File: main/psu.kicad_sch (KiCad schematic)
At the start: 33 parts, among them U401 TSV911xxLx, U402 LMR51430, U403 LDK130M33R, U404 LM317_SOT-223

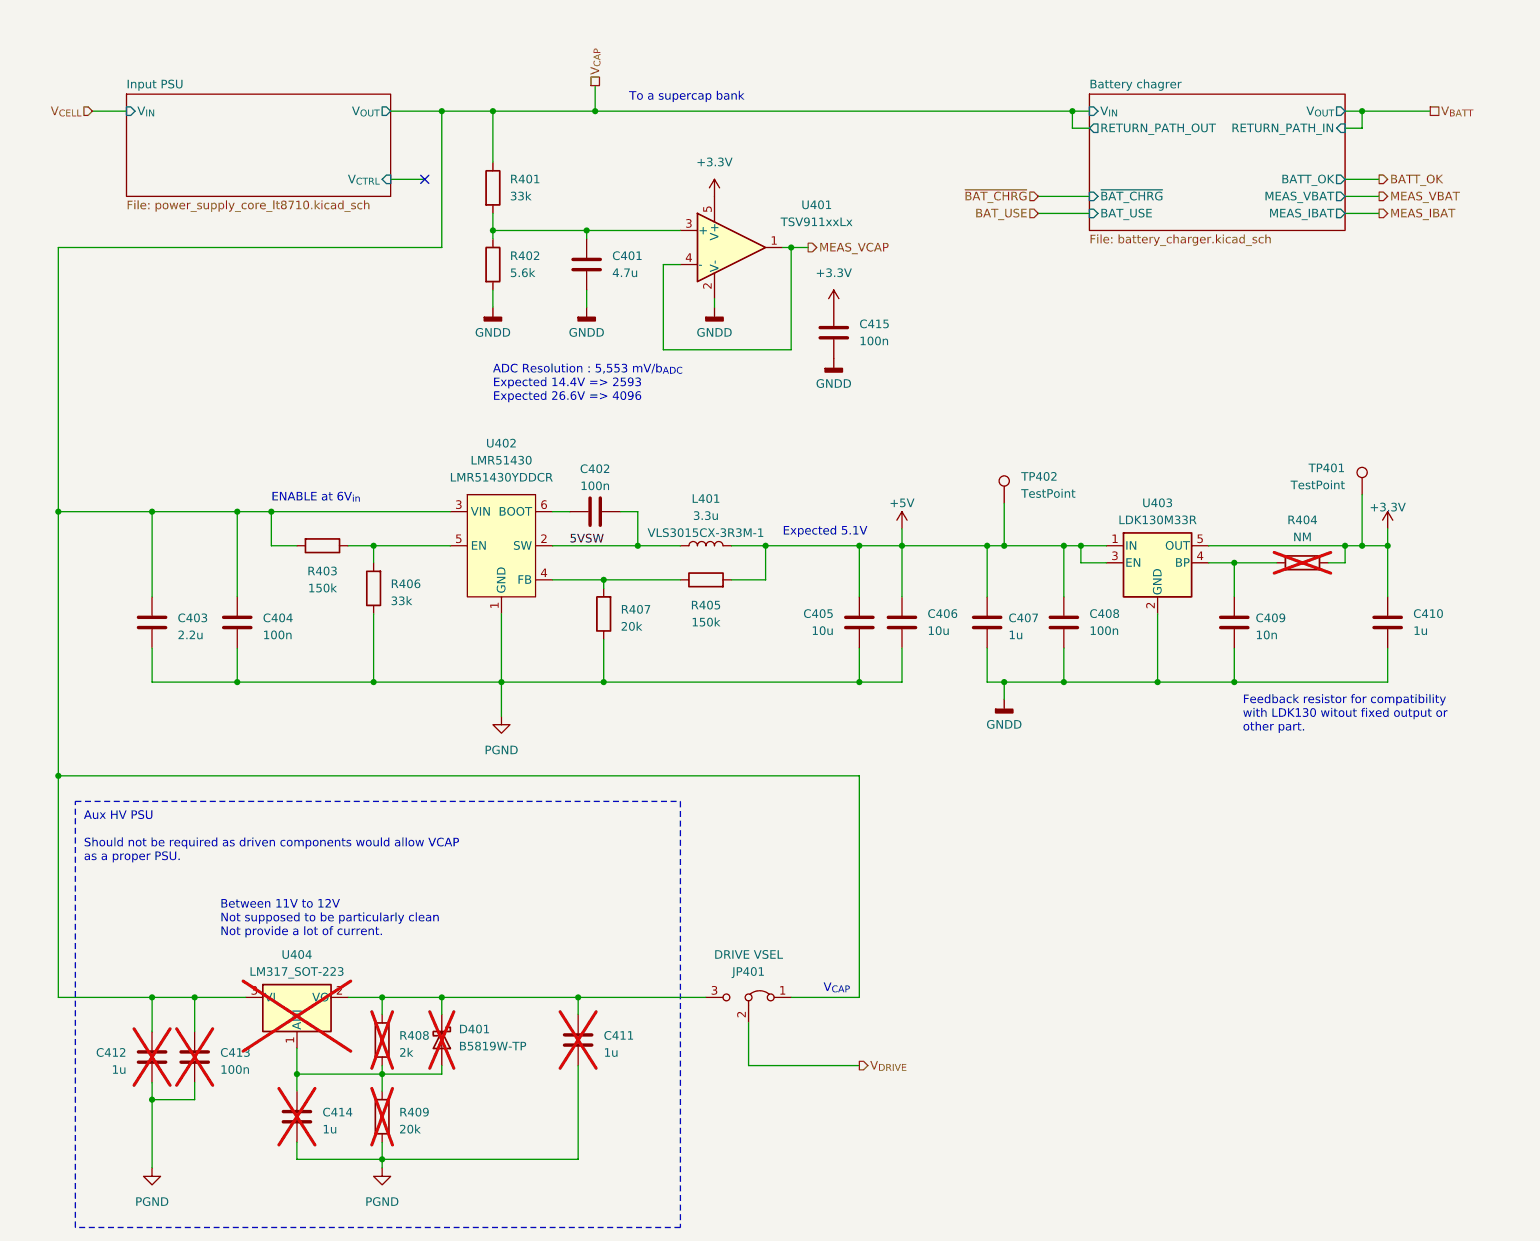
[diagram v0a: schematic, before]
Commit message: Clean silkscreen
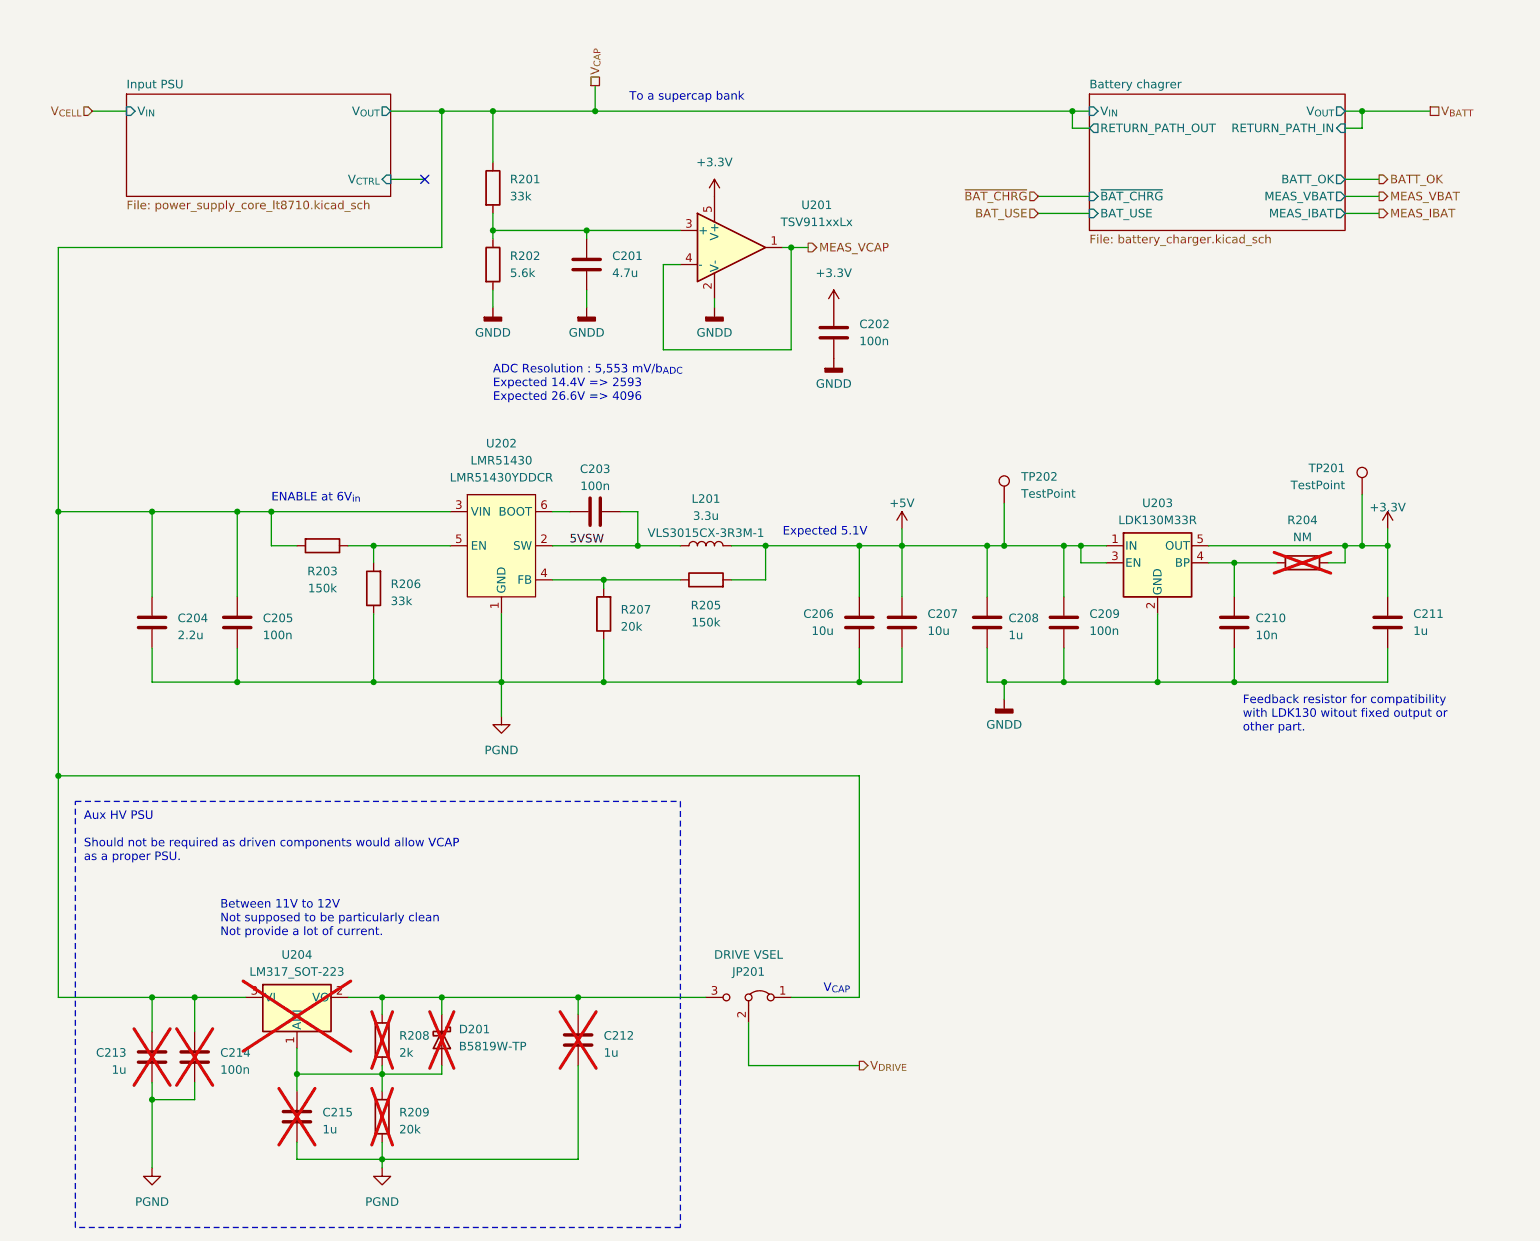
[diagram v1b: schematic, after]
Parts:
- renumbered C401 to C201, C415 to C202, C402 to C203, C403 to C204, C404 to C205, C405 to C206, C406 to C207, C407 to C208, C408 to C209, C409 to C210, C410 to C211, C411 to C212, C412 to C213, C413 to C214, C414 to C215, D401 to D201, JP401 to JP201, L401 to L201, R401 to R201, R402 to R202, R403 to R203, R404 to R204, R405 to R205, R406 to R206, R407 to R207, R408 to R208, R409 to R209, TP401 to TP201, TP402 to TP202, U401 to U201, U402 to U202, U403 to U203, U404 to U204

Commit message: Tapeout
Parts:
- added TP203: TestPoint, TestPoint:TestPoint_Keystone_5010-5014_Multipurpose, symbol Connector:TestPoint
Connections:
- net GNDD: now also TP203.1
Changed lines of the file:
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@@
 	(wire
 		(pts
+			(xy 232.41 86.36) (xy 232.41 88.9)
+		)
+		(stroke
+			(width 0)
+			(type default)
+		)
+	)
+	(wire
+		(pts
 			(xy 66.04 93.98) (xy 77.47 93.98)
 		)
@@
 	(symbol
 		(lib_id "power:GNDD")
+		(at 232.41 88.9 0)
+		(unit 1)
+		(exclude_from_sim no)
+		(in_bom yes)
+		(on_board yes)
+		(dnp no)
+		(fields_autoplaced yes)
+		(property "Reference" "#PWR0213"
+			(at 232.41 95.25 0)
+			(effects
+				(font
+					(size 1.27 1.27)
+				)
+				(hide yes)
+			)
+		)
+		(property "Value" "GNDD"
+			(at 232.41 92.71 0)
+			(effects
+				(font
+					(size 1.27 1.27)
+				)
+			)
+		)
+		(property "Footprint" ""
+			(at 232.41 88.9 0)
+			(effects
+				(font
+					(size 1.27 1.27)
+				)
+				(hide yes)
+			)
+		)
+		(property "Datasheet" ""
+			(at 232.41 88.9 0)
+			(effects
+				(font
+					(size 1.27 1.27)
+				)
+				(hide yes)
+			)
+		)
+		(property "Description" "Power symbol creates a global label with name \"GNDD\" , digital ground"
+			(at 232.41 88.9 0)
+			(effects
+				(font
+					(size 1.27 1.27)
+				)
+				(hide yes)
+			)
+		)
+		(pin "1"
+		)
+		(instances
+			(project "dsv4"
+				(path "/c07e9297-fde8-4755-803e-d05072cd6096/164e5be8-13e0-4d66-ab9d-977f2147e774"
+					(reference "#PWR0213")
+					(unit 1)
+				)
+			)
+		)
+	)
+	(symbol
+		(lib_id "power:GNDD")
 		(at 134.62 66.04 0)
 		(unit 1)
@@
 					(unit 1)
 				)
+			)
+		)
+	)
+	(symbol
+		(lib_id "Connector:TestPoint")
+		(at 232.41 86.36 0)
+		(unit 1)
+		(exclude_from_sim no)
+		(in_bom yes)
+		(on_board yes)
+		(dnp no)
+		(fields_autoplaced yes)
+		(property "Reference" "TP203"
+			(at 229.87 82.423 0)
+			(effects
+				(font
+					(size 1.27 1.27)
+				)
+				(justify right)
+			)
+		)
+		(property "Value" "TestPoint"
+			(at 229.87 84.963 0)
+			(effects
+				(font
+					(size 1.27 1.27)
+				)
+				(justify right)
+			)
+		)
+		(property "Footprint" "TestPoint:TestPoint_Keystone_5010-5014_Multipurpose"
+			(at 237.49 86.36 0)
+			(effects
+				(font
+					(size 1.27 1.27)
+				)
+				(hide yes)
+			)
+		)
+		(property "Datasheet" "~"
+			(at 237.49 86.36 0)
+			(effects
+				(font
+					(size 1.27 1.27)
+				)
+				(hide yes)
+			)
+		)
+		(property "Description" ""
+			(at 232.41 86.36 0)
+			(effects
+				(font
+					(size 1.27 1.27)
+				)
+				(hide yes)
+			)
+		)
+		(property "MPN" ""
+			(at 232.41 86.36 0)
+			(effects
+				(font
+					(size 1.27 1.27)
+				)
+			)
+		)
+		(property "Mouser SKU" ""
+			(at 232.41 86.36 0)
+			(effects
+				(font
+					(size 1.27 1.27)
+				)
+				(hide yes)
+			)
+		)
+		(property "Notes" ""
+			(at 232.41 86.36 0)
+			(effects
+				(font
+					(size 1.27 1.27)
+				)
+				(hide yes)
+			)
+		)
+		(pin "1"
+		)
+		(instances
+			(project "dsv4"
+				(path "/c07e9297-fde8-4755-803e-d05072cd6096/164e5be8-13e0-4d66-ab9d-977f2147e774"
+					(reference "TP203")
+					(unit 1)
+				)

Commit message: Sent to fab
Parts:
- C201: MPN (none) -> CL21B475KAFNNNE; Mouser SKU (none) -> 187-CL21B475KAFNNNE
- C202, C205, C209: MPN (none) -> CL21B104KACNFNC; Mouser SKU (none) -> 187-CL21B104KACNFNC
- C203: MPN 0805YC104M4T2A -> CL21B104KACNFNC; Mouser SKU 581-0805YC104M4T2A -> 187-CL21B104KACNFNC
- C204: value 2.2u -> 10u; MPN (none) -> CL21A106KBYQNNE; Mouser SKU (none) -> 187-CL21A106KBYQNNE
- C206, C207: MPN (none) -> CL21A106KBYQNNE; Mouser SKU (none) -> 187-CL21A106KBYQNNE
- C208: MPN (none) -> CL21B105KLFVPNE; Mouser SKU (none) -> 187-CL21B105KLFVPNE
- C210: MPN (none) -> CL21B103KCANNND; Mouser SKU (none) -> 187-CL21B103KCANNND
- C211: value 1u -> 10u; MPN (none) -> CL21A106KBYQNNE; Mouser SKU (none) -> 187-CL21A106KBYQNNE

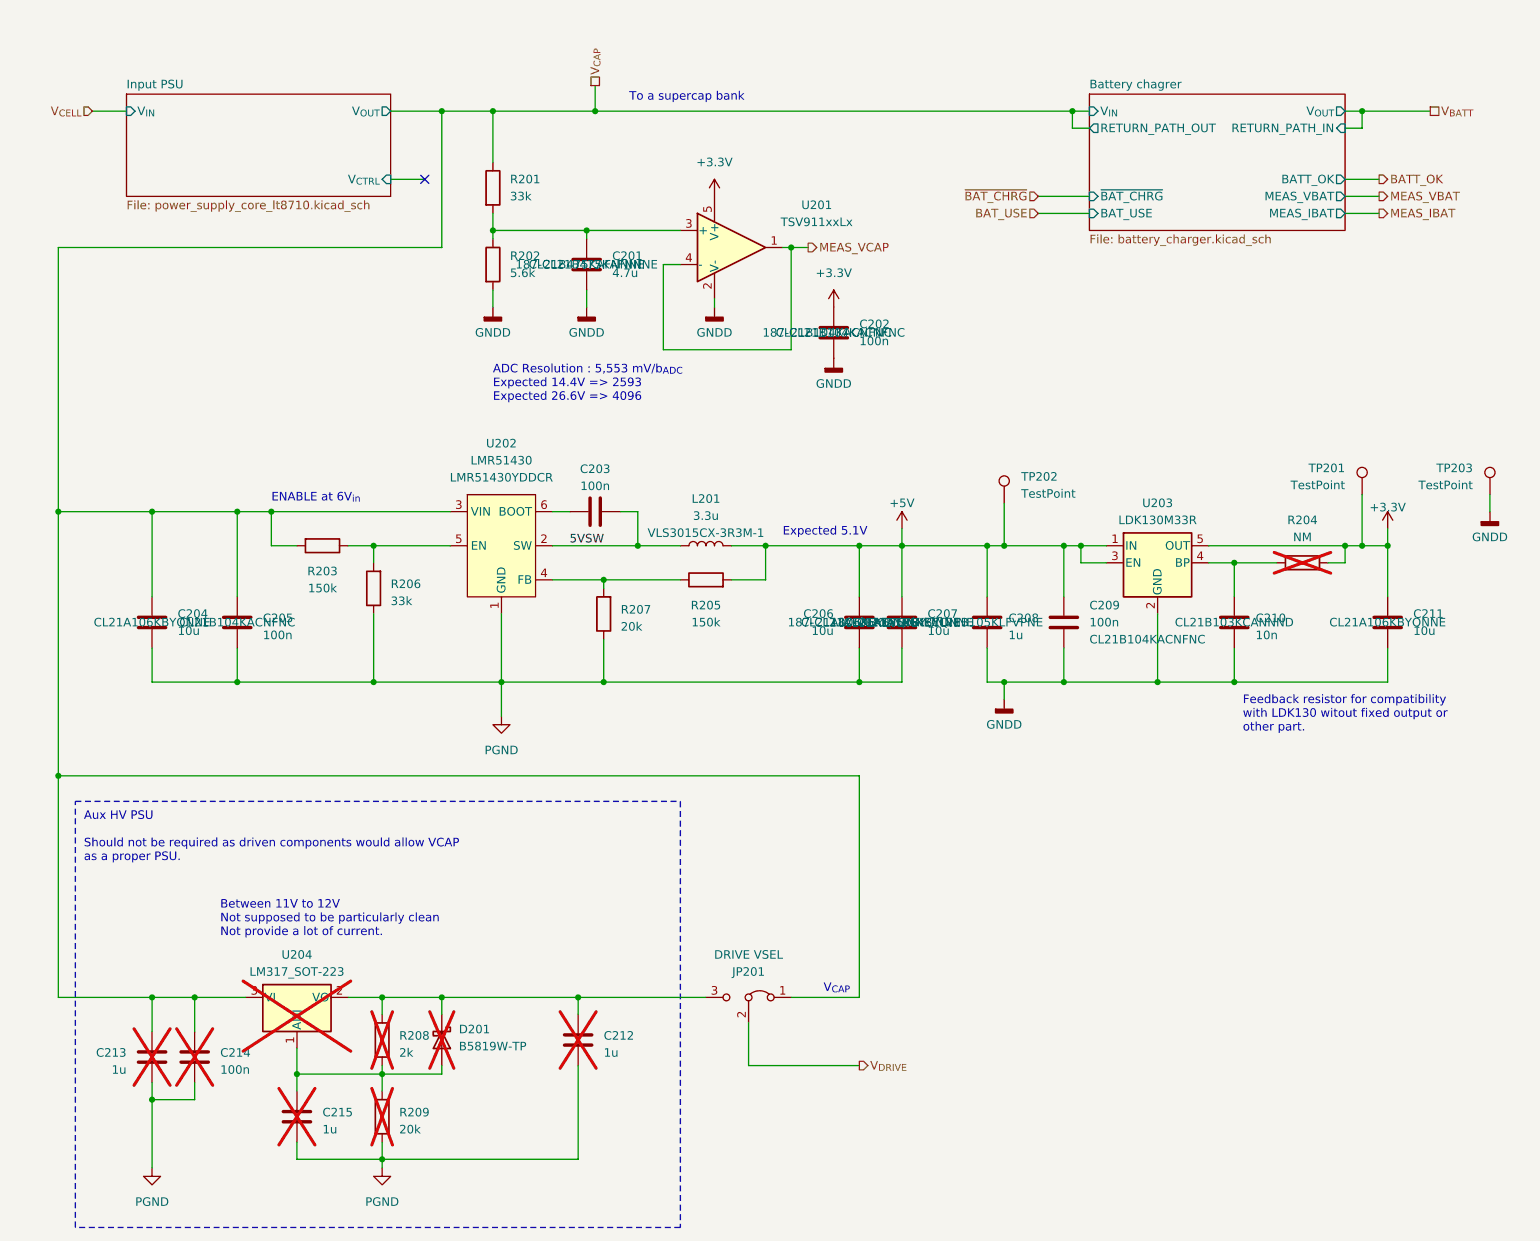
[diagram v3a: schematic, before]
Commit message: BOM almost OK, starts new side board.
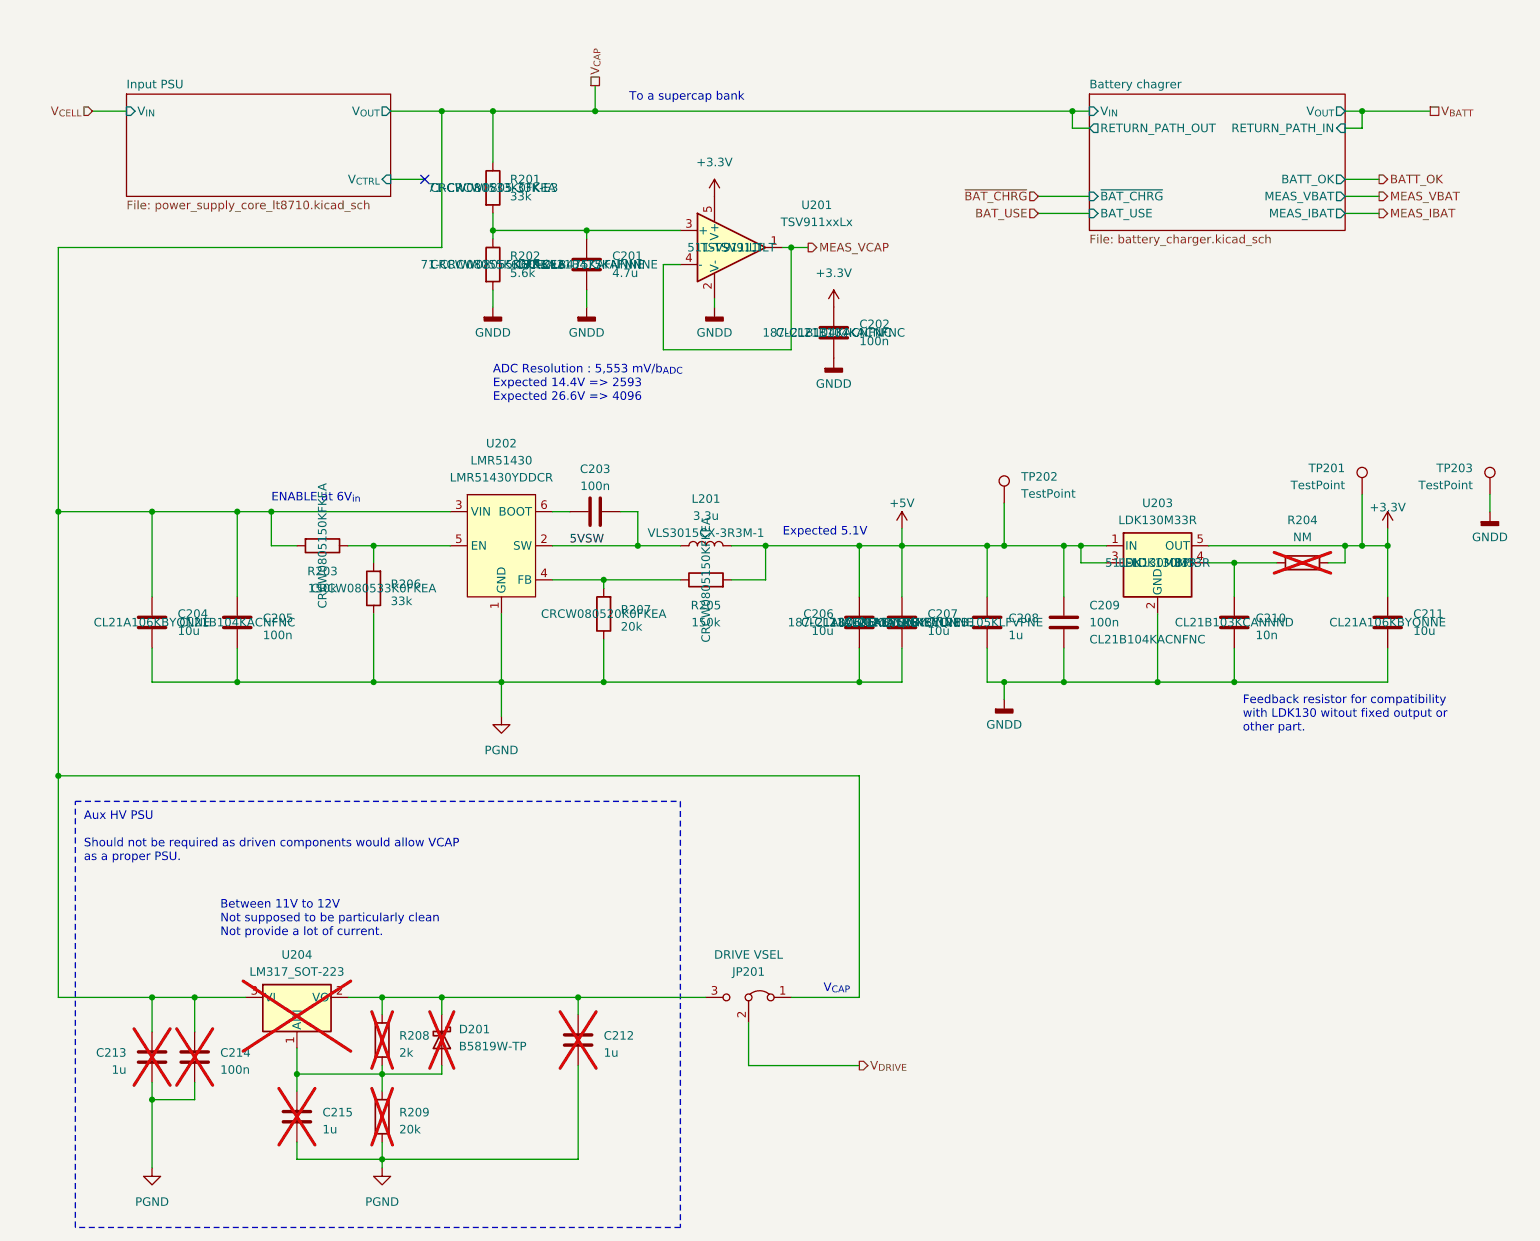
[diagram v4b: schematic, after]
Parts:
- JP201: now left out of the parts list
- R201, R206: MPN (none) -> CRCW080533K0FKEA; Mouser SKU (none) -> 71-CRCW0805-33K-E3
- R202: MPN (none) -> CRCW08055K60FKEA; Mouser SKU (none) -> 71-CRCW08055K60FKEA
- R203, R205: MPN (none) -> CRCW0805150KFKEA; Mouser SKU (none) -> 71-CRCW0805-150K-E3
- R207: MPN (none) -> CRCW080520K0FKEA; Mouser SKU (none) -> 71-CRCW0805-20K-E3
- U201: MPN (none) -> TSV911ILT; Mouser SKU (none) -> 511-TSV911ILT
- U203: MPN (none) -> LDK130M33R; Mouser SKU (none) -> 511-LDK130M33R
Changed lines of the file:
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@@
 (kicad_sch
-	(version 20240101)
+	(version 20240417)
 	(generator "eeschema")
 	(generator_version "8.99")
@@
 			)
 		)
-		(property "Mouser SKU" ""
+		(property "Mouser SKU" " 71-CRCW0805-20K-E3 "
 			(at 100.33 104.14 0)
 			(effects
@@
 			)
 		)
+		(property "MPN" " CRCW080520K0FKEA "
+			(at 100.33 104.14 0)
+			(effects
+				(font
+					(size 1.27 1.27)
+				)
+			)
+		)
 		(pin "1"
 		)
@@
 			)
 		)
+		(property "MPN" "CRCW08055K60FKEA"
+			(at 83.82 52.07 0)
+			(effects
+				(font
+					(size 1.27 1.27)
+				)
+			)
+		)
+		(property "Mouser SKU" " 71-CRCW08055K60FKEA "
+			(at 83.82 52.07 0)
+			(effects
+				(font
+					(size 1.27 1.27)
+				)
+			)
+		)
 		(pin "2"
 		)
@@
 			)
 		)
+		(property "MPN" "LDK130M33R"
+			(at 182.88 96.52 0)
+			(effects
+				(font
+					(size 1.27 1.27)
+				)
+			)
+		)
+		(property "Mouser SKU" " 511-LDK130M33R "
+			(at 182.88 96.52 0)
+			(effects
+				(font
+					(size 1.27 1.27)
+				)
+			)
+		)
 		(pin "3"
 		)
@@
 			)
 		)
+		(property "MPN" " TSV911ILT "
+			(at 119.38 49.53 0)
+			(effects
+				(font
+					(size 1.27 1.27)
+				)
+			)
+		)
+		(property "Mouser SKU" " 511-TSV911ILT "
+			(at 119.38 49.53 0)
+			(effects
+				(font
+					(size 1.27 1.27)
+				)
+			)
+		)
 		(pin "4"
 		)
@@
 			)
 		)
-		(property "Mouser SKU" ""
+		(property "Mouser SKU" " 71-CRCW0805-150K-E3 "
 			(at 115.57 99.06 0)
 			(effects
@@
 			)
 		)
+		(property "MPN" "CRCW0805150KFKEA"
+			(at 115.57 99.06 0)
+			(effects
+				(font
+					(size 1.27 1.27)
+				)
+			)
+		)
 		(pin "1"
 		)
@@
 		(unit 1)
 		(exclude_from_sim no)
-		(in_bom yes)
+		(in_bom no)
 		(on_board yes)
 		(dnp no)
@@
 			)
 		)
-		(property "Mouser SKU" ""
+		(property "Mouser SKU" " 71-CRCW0805-33K-E3 "
 			(at 66.04 100.33 0)
 			(effects
@@
 			)
 		)
+		(property "MPN" "CRCW080533K0FKEA"
+			(at 66.04 100.33 0)
+			(effects
+				(font
+					(size 1.27 1.27)
+				)
+			)
+		)
 		(pin "1"
 		)
@@
 			)
 		)
-		(property "Mouser SKU" ""
+		(property "Mouser SKU" " 71-CRCW0805-150K-E3 "
 			(at 58.42 93.98 0)
 			(effects
@@
 			)
 		)
+		(property "MPN" "CRCW0805150KFKEA"
+			(at 58.42 93.98 0)
+			(effects
+				(font
+					(size 1.27 1.27)
+				)
+			)
+		)
 		(pin "1"
 		)
@@
 			(at 83.82 40.64 0)
 			(effects
+				(font
+					(size 1.27 1.27)
+				)
+			)
+		)
+		(property "MPN" "CRCW080533K0FKEA"
+			(at 83.82 40.64 0)
+			(effects
+				(font
+					(size 1.27 1.27)
+				)
+			)
+		)
+		(property "Mouser SKU" " 71-CRCW0805-33K-E3 "
+			(at 83.82 40.64 0)
+			(effects
